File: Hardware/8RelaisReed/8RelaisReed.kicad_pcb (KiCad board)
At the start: 2 copper layers, 81.3 x 59.7 mm, 28 parts, among them J1 ISP, P1 5VIN, P10 CONN_01X02, P11 CONN_01X02, P4 CONN_01X02, P5 CONN_01X02, P6 CONN_01X02, P7 CONN_01X02, P8 CONN_01X02, P9 CONN_01X02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

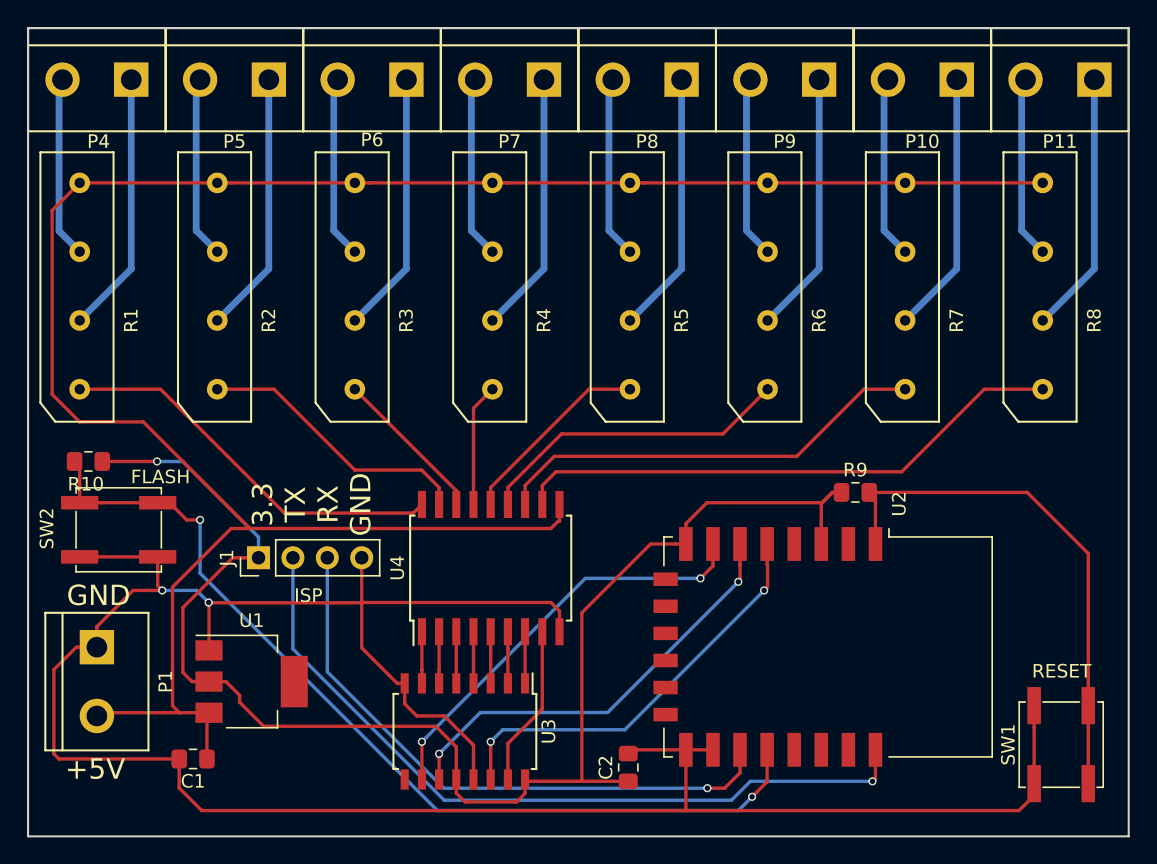
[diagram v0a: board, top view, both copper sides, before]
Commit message: - Modified almost all hardware boards : They were missing a pull-up resistor on GPIO2, which made impossible to flash. - Updated baseBoard.* files
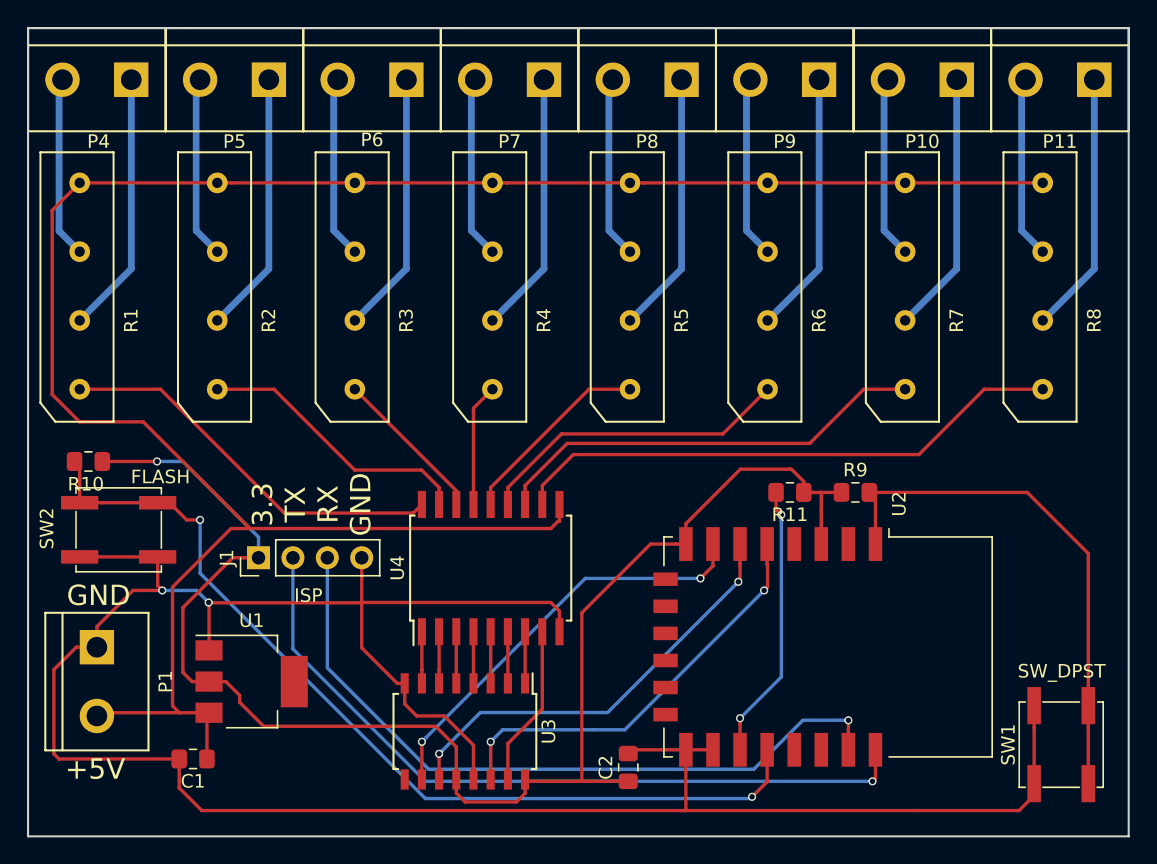
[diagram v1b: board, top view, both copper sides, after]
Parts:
- added R11: 10K, Resistor_SMD:R_0805_2012Metric_Pad1.15x1.40mm_HandSolder, F.Cu at (194.7, 100.3)
- SW1: value RESET -> SW_DPST
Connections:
- U2 pad 10: Net-(U2-Pad10) -> (no net)
- U2 pad 11: Net-(U2-Pad11) -> (no net)
- U2 pad 12: Net-(U2-Pad12) -> (no net)
- U2 pad 13: Net-(U2-Pad13) -> (no net)
- U2 pad 14: Net-(U2-Pad14) -> (no net)
- U2 pad 17: /RXD -> Net-(R11-Pad2)
- U2 pad 19: Net-(U2-Pad19) -> (no net)
- U2 pad 2: Net-(U2-Pad2) -> (no net)
- U2 pad 20: Net-(U2-Pad20) -> (no net)
- U2 pad 21: Net-(U2-Pad21) -> /RXD
- U2 pad 4: Net-(U2-Pad4) -> (no net)
- U2 pad 9: Net-(U2-Pad9) -> (no net)
- U3 pad 9: Net-(U3-Pad9) -> (no net)
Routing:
- net Net-(R11-Pad2): track 0.00 -> 20.0 mm, vias 0 -> 2
- net /RXD: track 44.6 -> 53.4 mm
- net /3V3: track 108.1 -> 109.7 mm
- net /TXD: track 57.2 -> 56.0 mm
- net Net-(R10-Pad2): track 68.9 -> 68.2 mm

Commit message: Fix on the BaseBoard class
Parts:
- removed C1, C2: 10uF, Capacitor_SMD:C_0805_2012Metric_Pad1.15x1.40mm_HandSolder
- removed P1: 5VIN, Connectors:bornier2
- removed R10, R11, R9: 10K, Resistor_SMD:R_0805_2012Metric_Pad1.15x1.40mm_HandSolder
- removed SW1: SW_DPST, Button_Switch_SMD:SW_SPST_EVPBF
- removed SW2: FLASH, Button_Switch_SMD:SW_SPST_EVPBF
- removed U1: AMS1117, TO_SOT_Packages_SMD:SOT-223
- removed U2: ESP-12F, RF_Module:ESP-12E
- J1: value ISP -> Conn_02x03_Odd_Even; footprint Connector_PinHeader_2.54mm:PinHeader_1x04_P2.54mm_Vertical -> Connector_PinHeader_2.54mm:PinHeader_2x03_P2.54mm_Vertical
- moved J1 37.2 mm to (192.6, 105.9), turned to 270 degrees
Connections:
- J1 pad 1: /3V3 -> /5V
- J1 pad 2: /TXD -> /SER
- J1 pad 3: /RXD -> /SRCLK
- J1 pad 4: /GND -> /RCLK
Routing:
- net /GND: track 175.6 -> 0.00 mm, vias 2 -> 0
- net /3V3: track 109.7 -> 28.5 mm, vias 1 -> 0
- net Net-(R10-Pad2): track 68.2 -> 0.00 mm, vias 2 -> 0
- net /TXD: track 56.0 -> 0.00 mm, vias 1 -> 0
- net /RXD: track 53.4 -> 0.00 mm, vias 1 -> 0
- net Net-(R9-Pad2): track 39.0 -> 0.00 mm
- net /5V: track 159.5 -> 135.0 mm
- net Net-(R11-Pad2): track 20.0 -> 0.00 mm, vias 2 -> 0
- net /SER: track 31.2 -> 28.1 mm, vias 2 -> 1
- net /SRCLK: track 32.1 -> 30.9 mm, vias 2 -> 1
- net /S2: track 11.6 -> 12.7 mm
- net /S1: track 20.6 -> 21.5 mm
- net /S0: track 29.3 -> 28.8 mm
- net /RCLK: track 31.3 -> 31.8 mm, vias 2 -> 1
- added copper zone on F.Cu, net /GND
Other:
- board text removed: "+5V"
- board text removed: "3.3 TX RX GND"
- board text removed: "GND"
